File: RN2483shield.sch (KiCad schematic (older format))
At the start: 28 parts, among them J1 LoRa_GPIO, J2 SMA_HF, J3 SMA_LF, Q1 BSS138, Q2 BSS138, U1 RN2483/RN2903

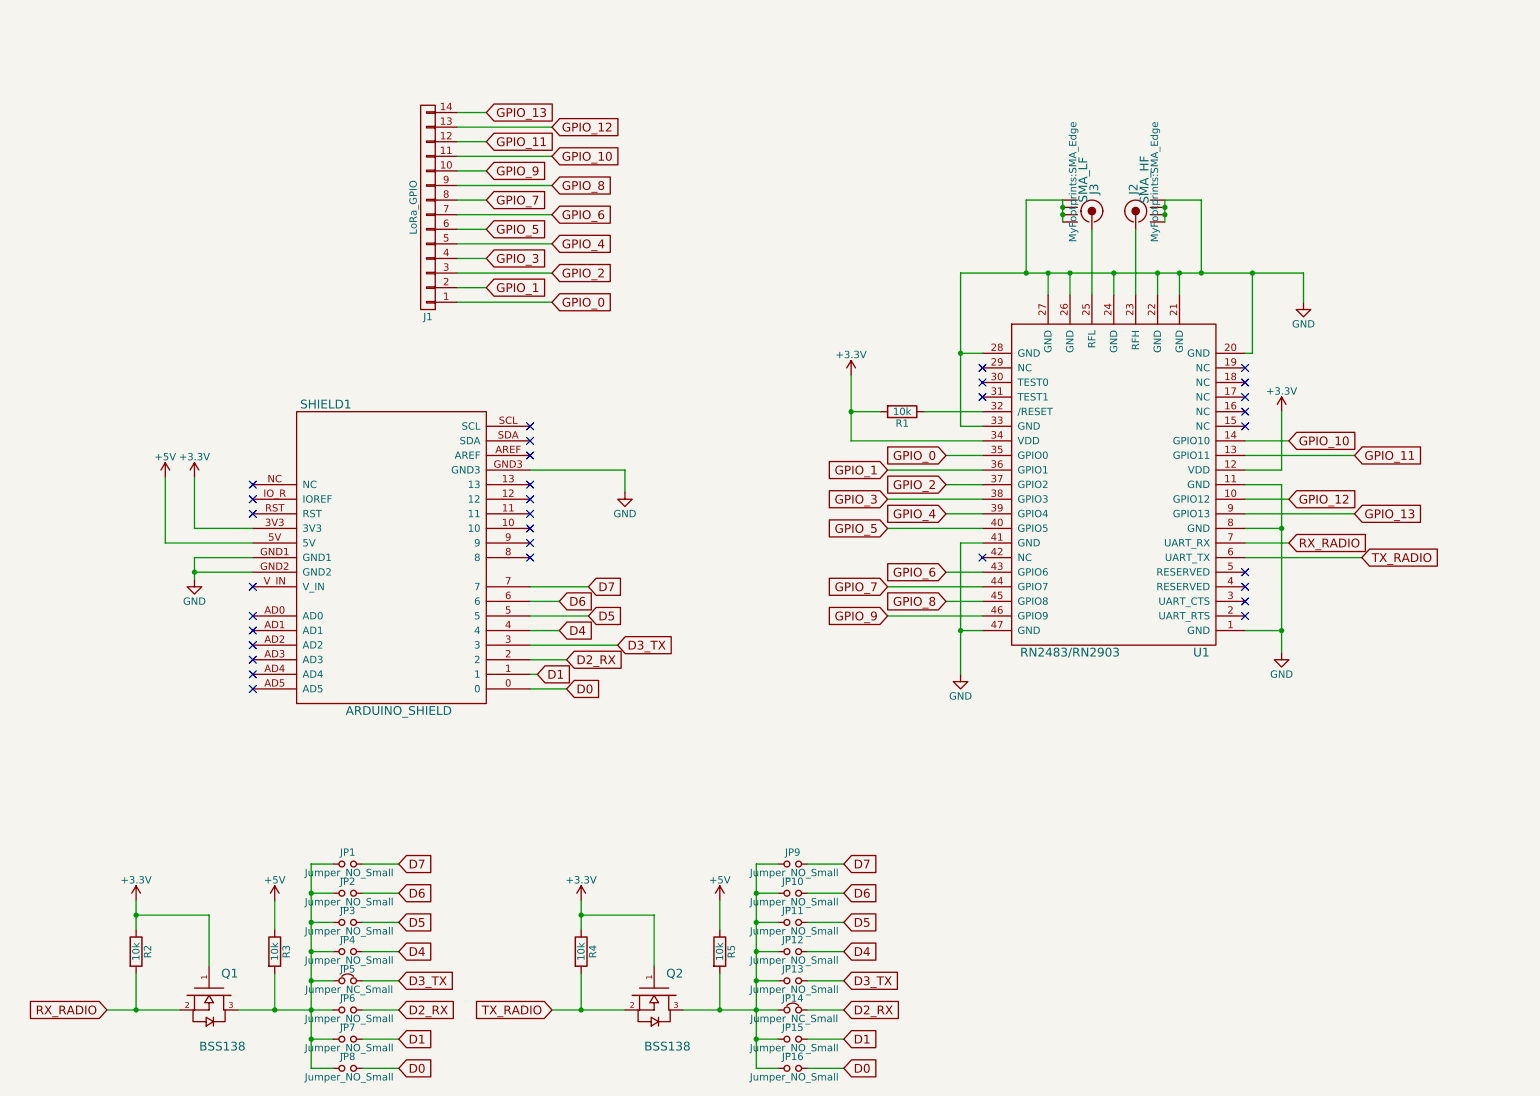
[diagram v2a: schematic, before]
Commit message: removed freetronics libraries
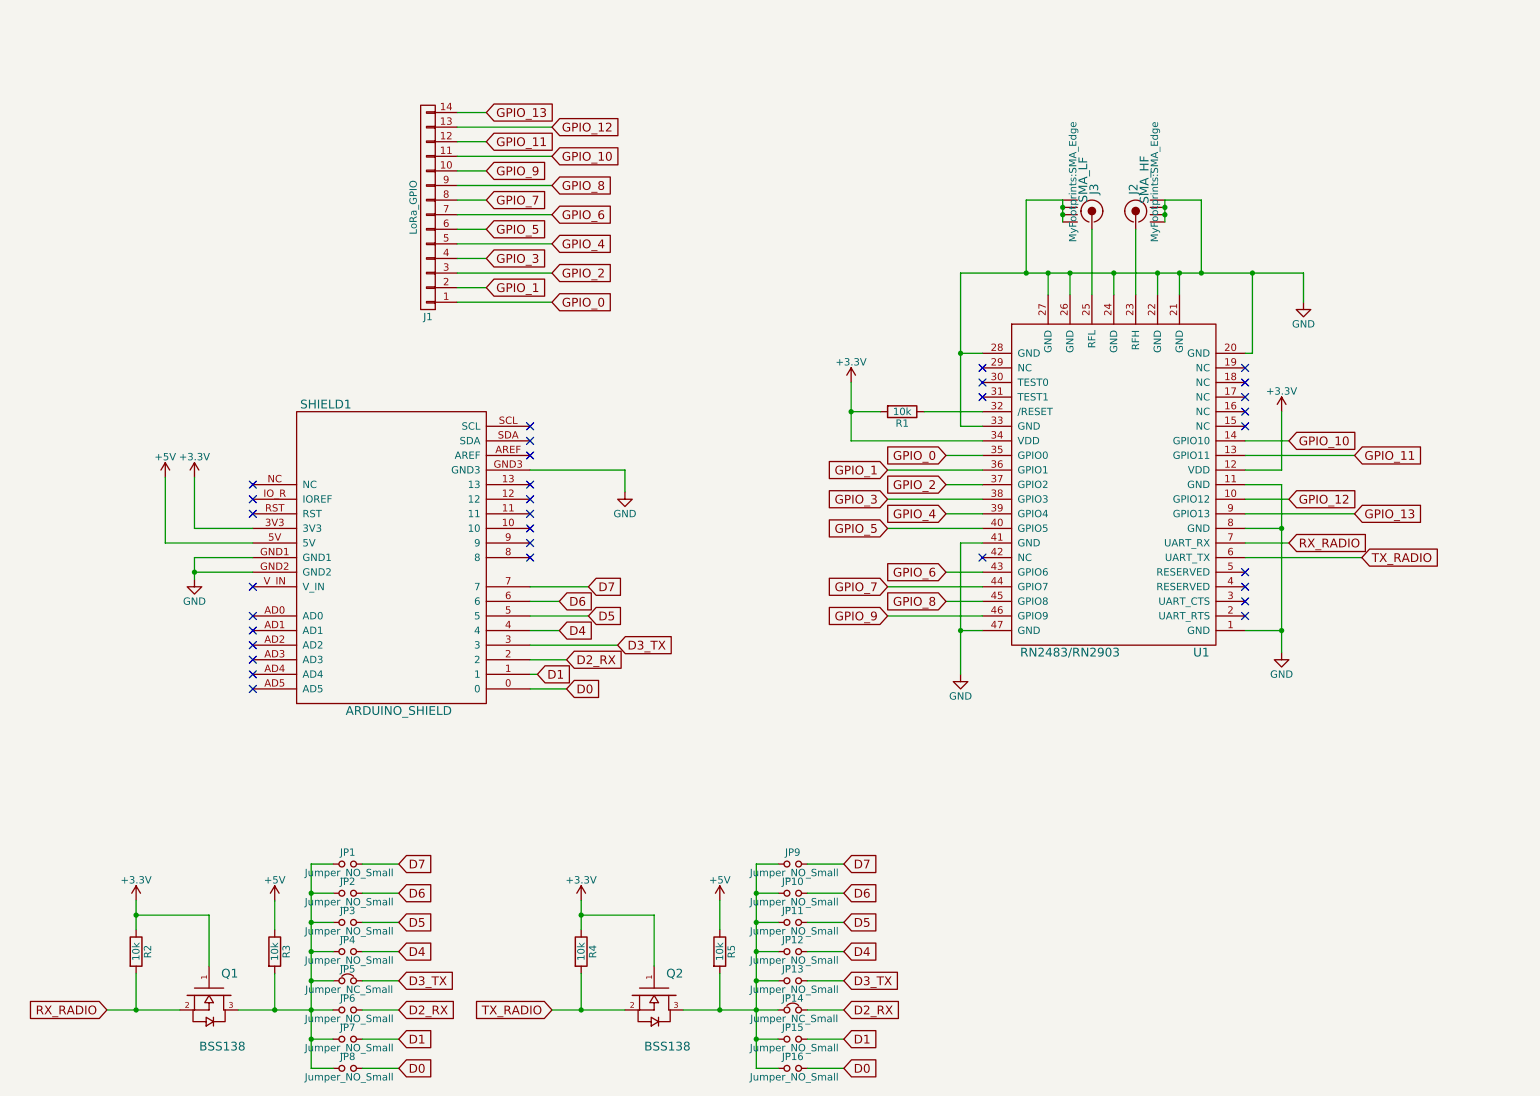
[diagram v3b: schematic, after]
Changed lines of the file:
@@
 LIBS:valves
 LIBS:rn2483
-LIBS:freetronics_schematic
 LIBS:screw_terminal
 LIBS:sma_through
@@
 L +3.3V #PWR01
 U 1 1 593429C3
-P 6400 2750
-F 0 "#PWR01" H 6400 2600 50  0001 C CNN
-F 1 "+3.3V" H 6400 2890 50  0000 C CNN
-F 2 "" H 6400 2750 50  0001 C CNN
-F 3 "" H 6400 2750 50  0001 C CNN
-	1    6400 2750
+P 6400 2800
+F 0 "#PWR01" H 6400 2650 50  0001 C CNN
+F 1 "+3.3V" H 6400 2940 50  0000 C CNN
+F 2 "" H 6400 2800 50  0001 C CNN
+F 3 "" H 6400 2800 50  0001 C CNN
+	1    6400 2800
 	1    0    0    -1
 $EndComp
@@
 $EndComp
 Wire Wire Line
-	8550 1550 8550 1700
+	8550 1550 8550 1600
+Wire Wire Line
+	8550 1600 8550 1650
+Wire Wire Line
+	8550 1650 8550 1700
 Connection ~ 8550 1600
 Connection ~ 8550 1650
@@
 	4200 3400 4850 3400
 Wire Wire Line
-	7850 1550 7850 1700
+	7850 1550 7850 1600
+Wire Wire Line
+	7850 1600 7850 1650
+Wire Wire Line
+	7850 1650 7850 1700
 Connection ~ 7850 1650
 Connection ~ 7850 1600
@@
 	2300 4000 1900 4000
 Wire Wire Line
-	1900 4000 1900 4150
+	1900 4000 1900 4100
+Wire Wire Line
+	1900 4100 1900 4150
 Wire Wire Line
 	2300 4100 1900 4100
@@
 	9350 4500 9100 4500
 Wire Wire Line
-	9350 3500 9350 4650
+	9350 3500 9350 3800
+Wire Wire Line
+	9350 3800 9350 4500
+Wire Wire Line
+	9350 4500 9350 4650
 Wire Wire Line
 	9100 3800 9350 3800
@@
 	7750 2050 7750 2200
 Wire Wire Line
-	7150 2050 9500 2050
+	7150 2050 7600 2050
+Wire Wire Line
+	7600 2050 7750 2050
+Wire Wire Line
+	7750 2050 7900 2050
+Wire Wire Line
+	7900 2050 8200 2050
+Wire Wire Line
+	8200 2050 8500 2050
+Wire Wire Line
+	8500 2050 8650 2050
+Wire Wire Line
+	8650 2050 8800 2050
+Wire Wire Line
+	8800 2050 9150 2050
+Wire Wire Line
+	9150 2050 9500 2050
 Wire Wire Line
 	9500 2050 9500 2250
@@
 	6400 3200 7300 3200
 Wire Wire Line
-	6400 2750 6400 3200
+	6400 2800 6400 3000
+Wire Wire Line
+	6400 3000 6400 3200
 Wire Wire Line
 	7300 3000 6900 3000
@@
 	7300 2600 7150 2600
 Wire Wire Line
-	7150 2050 7150 3100
+	7150 2050 7150 2600
+Wire Wire Line
+	7150 2600 7150 3100
 Wire Wire Line
 	7150 3100 7300 3100
@@
 	7300 4500 7150 4500
 Wire Wire Line
-	7150 3900 7150 4800
+	7150 3900 7150 4500
+Wire Wire Line
+	7150 4500 7150 4800
 Wire Wire Line
 	7300 3900 7150 3900
@@
 NoConn ~ 4200 4000
 Wire Wire Line
-	1300 7100 1800 7100
+	1300 7100 1500 7100
+Wire Wire Line
+	1500 7100 1800 7100
 Wire Wire Line
 	1500 6850 1500 7100
 Connection ~ 1500 7100
 Wire Wire Line
-	1500 6350 1500 6550
+	1500 6350 1500 6450
+Wire Wire Line
+	1500 6450 1500 6550
 Wire Wire Line
 	2450 6350 2450 6550
 Wire Wire Line
-	2200 7100 2850 7100
+	2200 7100 2450 7100
+Wire Wire Line
+	2450 7100 2700 7100
+Wire Wire Line
+	2700 7100 2850 7100
 Wire Wire Line
 	2450 6850 2450 7100
@@
 	2700 6900 2850 6900
 Wire Wire Line
-	2700 6100 2700 7500
+	2700 6100 2700 6300
+Wire Wire Line
+	2700 6300 2700 6500
+Wire Wire Line
+	2700 6500 2700 6700
+Wire Wire Line
+	2700 6700 2700 6900
+Wire Wire Line
+	2700 6900 2700 7100
+Wire Wire Line
+	2700 7100 2700 7300
+Wire Wire Line
+	2700 7300 2700 7500
 Connection ~ 2700 7100
 Wire Wire Line
@@
 $EndComp
 Wire Wire Line
-	4350 7100 4850 7100
+	4350 7100 4550 7100
+Wire Wire Line
+	4550 7100 4850 7100
 Wire Wire Line
 	4550 6850 4550 7100
 Connection ~ 4550 7100
 Wire Wire Line
-	4550 6350 4550 6550
+	4550 6350 4550 6450
+Wire Wire Line
+	4550 6450 4550 6550
 Wire Wire Line
 	5500 6350 5500 6550
 Wire Wire Line
-	5250 7100 5900 7100
+	5250 7100 5500 7100
+Wire Wire Line
+	5500 7100 5750 7100
+Wire Wire Line
+	5750 7100 5900 7100
 Wire Wire Line
 	5500 6850 5500 7100
@@
 	5750 6900 5900 6900
 Wire Wire Line
-	5750 6100 5750 7500
+	5750 6100 5750 6300
+Wire Wire Line
+	5750 6300 5750 6500
+Wire Wire Line
+	5750 6500 5750 6700
+Wire Wire Line
+	5750 6700 5750 6900
+Wire Wire Line
+	5750 6900 5750 7100
+Wire Wire Line
+	5750 7100 5750 7300
+Wire Wire Line
+	5750 7300 5750 7500
 Connection ~ 5750 7100
 Wire Wire Line

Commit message: EOD: redrafted board with new level shifters
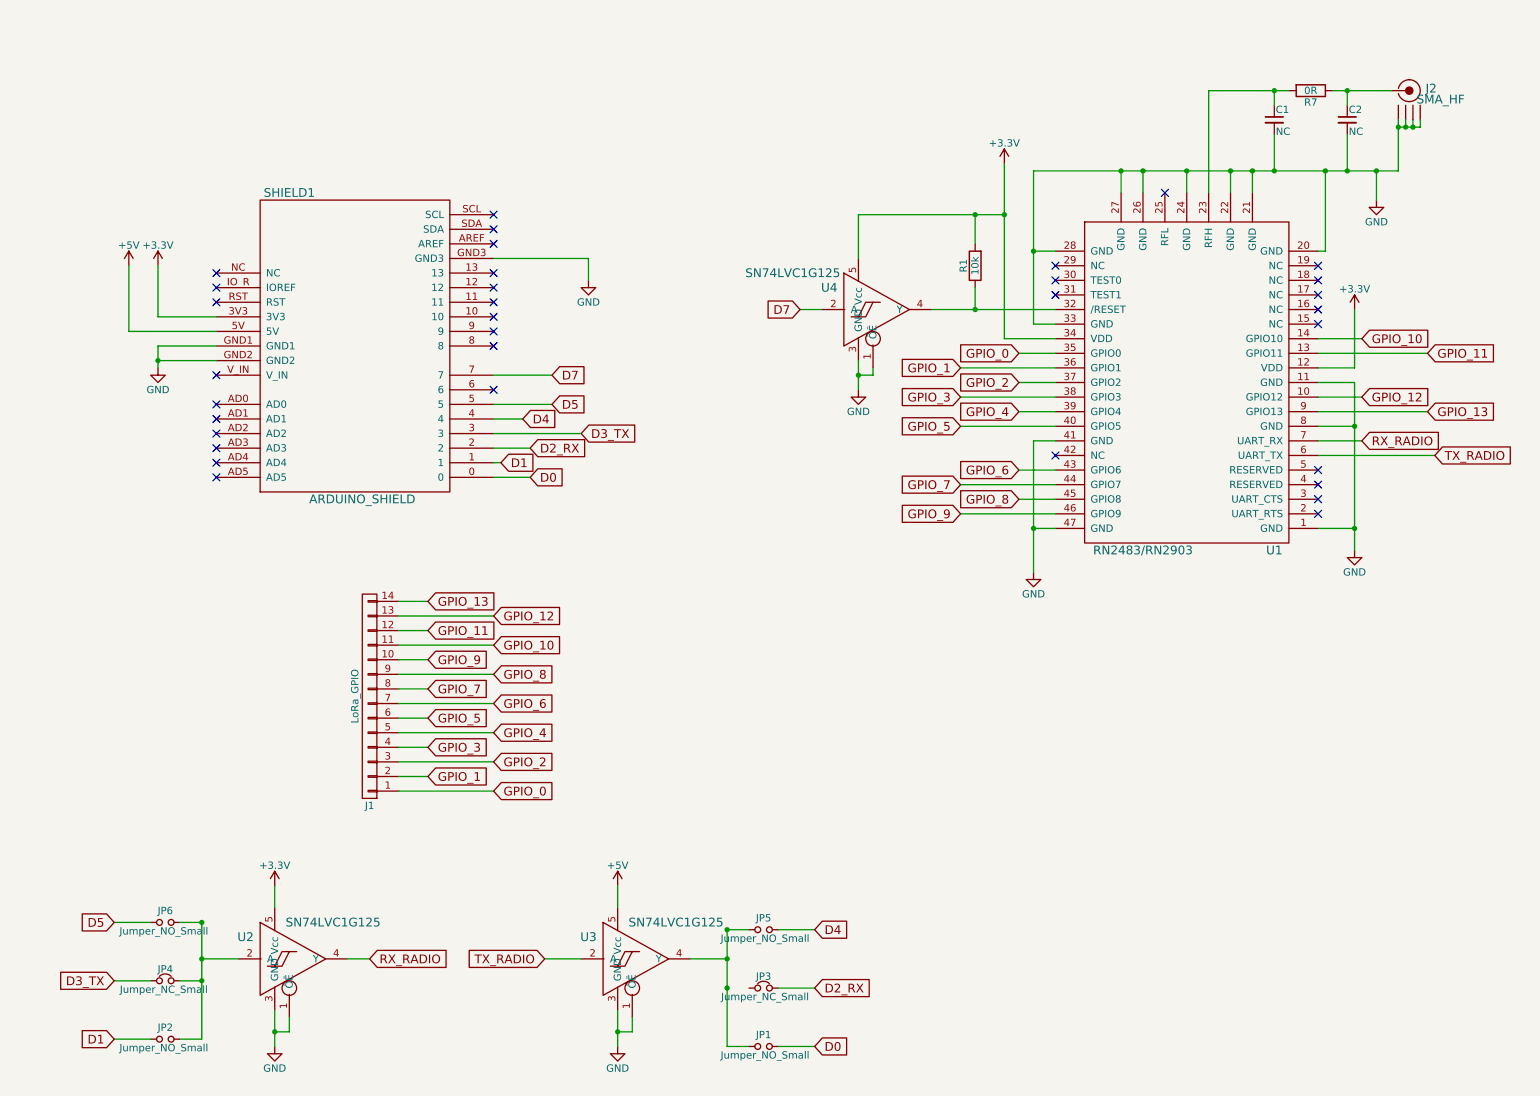
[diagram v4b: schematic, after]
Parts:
- removed J3: SMA_LF, MyFootprints:SMA_Edge, symbol SMA
- removed JP1, JP10, JP11, JP13, JP15, JP2, JP4, JP6, JP8, JP9: Jumper_NO_Small, MyFootprints:NO_SMD_JPR, symbol Jumper_NO_Small
- removed Q1, Q2: BSS138, TO_SOT_Packages_SMD:SOT-23, symbol MOSFET_N_GSD
- removed R2, R3, R4, R5: 10k, Resistors_SMD:R_0603_HandSoldering, symbol R
- added C1, C2: NC, Resistors_SMD:R_0603, symbol C_Small
- added R7: 0R, Resistors_SMD:R_0603, symbol R
- added U2, U3, U4: SN74LVC1G125, TO_SOT_Packages_SMD:SOT-23-5, symbol SN74LVC1G125
- J2: footprint MyFootprints:SMA_Edge -> MyFootprints:multi-rf-sma-ufl
- R1: footprint Resistors_SMD:R_0603_HandSoldering -> Resistors_SMD:R_0603
- renumbered JP16 to JP1, JP7 to JP2, JP14 to JP3, JP5 to JP4, JP12 to JP5, JP3 to JP6
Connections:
- net +3V3: now also U2.5 (Vcc), U4.5 (Vcc)
- net +5V: now also U3.5 (Vcc)
- net D7: now also U4.2 (A)
- net GND: now also C1.2, C2.2, U2.1 (ŌĒ), U2.3 (GND), U3.1 (ŌĒ), U3.3 (GND), U4.1 (ŌĒ), U4.3 (GND)
- net RX_RADIO: now also U2.4 (Y)
- net TX_RADIO: now also U3.2 (A)
- net at U1.23 (RFH): now also C1.1, R7.2; no longer J2.1 (RF)
- net at R1.1, U1.32 (/RESET): now also U4.4 (Y)
- net at JP2.1, JP4.1, JP6.1: now also U2.2 (A)
- net at JP1.1, JP5.1: now also U3.4 (Y); no longer JP3.1
- net D6: no longer names the net of SHIELD1.6
- new net: C2.1, J2.1 (RF), R7.1
- no-connect marks 32 -> 34
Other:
- moved on the sheet: J1, J2, JP1, JP2, JP3, JP4, JP5, JP6, R1, SHIELD1, U1
